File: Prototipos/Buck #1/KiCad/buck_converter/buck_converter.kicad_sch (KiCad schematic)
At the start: 19 parts, among them J1 Screw_Terminal_01x02, J3 Screw_Terminal_01x02, J4 Conn_01x03_Pin, Q1 IRLZ44N, Q2 IRF9540NPBF

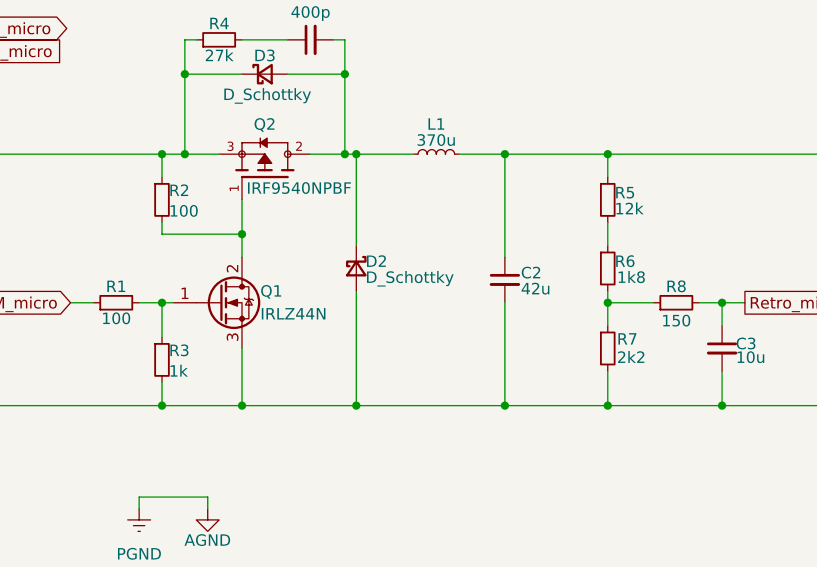
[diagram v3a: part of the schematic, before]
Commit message: Diseño del circuito final, agregado de nuevas librerías
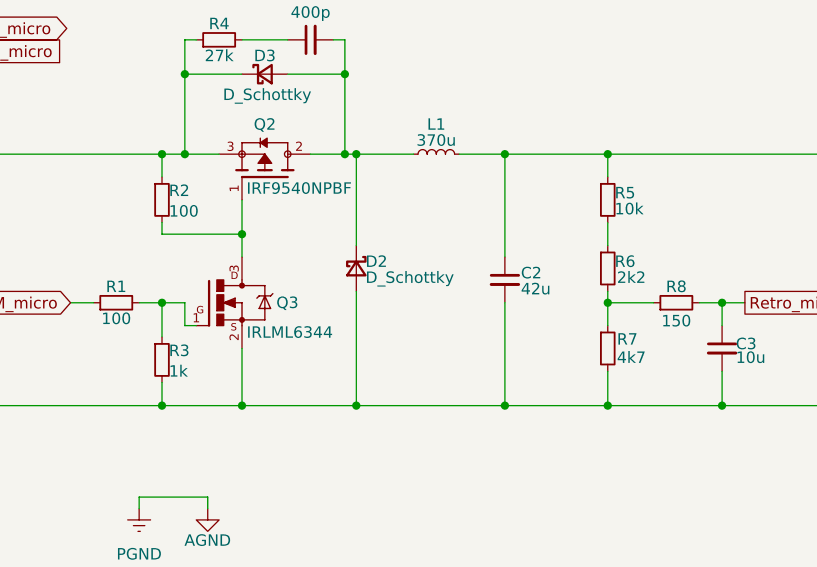
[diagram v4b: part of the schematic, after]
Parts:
- removed Q1: IRLZ44N, Package_TO_SOT_THT:TO-220-3_Vertical, symbol Transistor_FET:IRLZ44N
- added Q3: IRLML6344, IRLML6344:SOT23, symbol IRLML6344:IRLML6344
- R5: value 12k -> 10k
- R6: value 1k8 -> 2k2
- R7: value 2k2 -> 4k7
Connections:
- net AGND: now also Q3.2
- net at Q2.1, R2.2: now also Q3.3
- net at R1.2, R3.1: now also Q3.1
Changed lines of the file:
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@@
 	(wire
 		(pts
-			(xy 86.36 69.85) (xy 87.63 69.85)
+			(xy 86.36 69.85) (xy 88.9 69.85)
 		)
 		(stroke
@@
 	(wire
 		(pts
+			(xy 88.9 72.39) (xy 90.17 72.39)
+		)
+		(stroke
+			(width 0)
+			(type default)
+		)
+	)
+	(wire
+		(pts
 			(xy 135.89 60.96) (xy 135.89 63.5)
 		)
@@
 		(pts
 			(xy 148.59 69.85) (xy 148.59 72.39)
+		)
+		(stroke
+			(width 0)
+			(type default)
+		)
+	)
+	(wire
+		(pts
+			(xy 88.9 69.85) (xy 88.9 72.39)
 		)
 		(stroke
@@
 	)
 	(symbol
+		(lib_id "IRLML6344:IRLML6344")
+		(at 92.71 69.85 0)
+		(unit 1)
+		(exclude_from_sim no)
+		(in_bom yes)
+		(on_board yes)
+		(dnp no)
+		(property "Reference" "Q3"
+			(at 99.06 69.85 0)
+			(effects
+				(font
+					(size 1.27 1.27)
+				)
+				(justify left)
+			)
+		)
+		(property "Value" "IRLML6344"
+			(at 95.758 73.152 0)
+			(effects
+				(font
+					(size 1.27 1.27)
+				)
+				(justify left)
+			)
+		)
+		(property "Footprint" "IRLML6344:SOT23"
+			(at 92.71 69.85 0)
+			(effects
+				(font
+					(size 1.27 1.27)
+				)
+				(justify bottom)
+				(hide yes)
+			)
+		)
+		(property "Datasheet" ""
+			(at 92.71 69.85 0)
+			(effects
+				(font
+					(size 1.27 1.27)
+				)
+				(hide yes)
+			)
+		)
+		(property "Description" ""
+			(at 92.71 69.85 0)
+			(effects
+				(font
+					(size 1.27 1.27)
+				)
+				(hide yes)
+			)
+		)
+		(property "MF" "Infineon Technologies"
+			(at 92.71 69.85 0)
+			(effects
+				(font
+					(size 1.27 1.27)
+				)
+				(justify bottom)
+				(hide yes)
+			)
+		)
+		(property "Description_1" "Trans MOSFET N-CH 30V 5A 3-Pin SOT-23 T/R"
+			(at 92.71 69.85 0)
+			(effects
+				(font
+					(size 1.27 1.27)
+				)
+				(justify bottom)
+				(hide yes)
+			)
+		)
+		(property "Package" "None"
+			(at 92.71 69.85 0)
+			(effects
+				(font
+					(size 1.27 1.27)
+				)
+				(justify bottom)
+				(hide yes)
+			)
+		)
+		(property "Price" "None"
+			(at 92.71 69.85 0)
+			(effects
+				(font
+					(size 1.27 1.27)
+				)
+				(justify bottom)
+				(hide yes)
+			)
+		)
+		(property "SnapEDA_Link" "https://www.snapeda.com/parts/IRLML6344/Infineon/view-part/?ref=snap"
+			(at 92.71 69.85 0)
+			(effects
+				(font
+					(size 1.27 1.27)
+				)
+				(justify bottom)
+				(hide yes)
+			)
+		)
+		(property "MP" "IRLML6344"
+			(at 92.71 69.85 0)
+			(effects
+				(font
+					(size 1.27 1.27)
+				)
+				(justify bottom)
+				(hide yes)
+			)
+		)
+		(property "Availability" "Not in stock"
+			(at 92.71 69.85 0)
+			(effects
+				(font
+					(size 1.27 1.27)
+				)
+				(justify bottom)
+				(hide yes)
+			)
+		)
+		(property "Check_prices" "https://www.snapeda.com/parts/IRLML6344/Infineon/view-part/?ref=eda"
+			(at 92.71 69.85 0)
+			(effects
+				(font
+					(size 1.27 1.27)
+				)
+				(justify bottom)
+				(hide yes)
+			)
+		)
+		(pin "3"
+		)
+		(pin "2"
+		)
+		(pin "1"
+		)
+		(instances
+			(project ""
+				(path "/bb8bc01e-43dc-40c7-9cc7-76fd3e77d2b7"
+					(reference "Q3")
+					(unit 1)
+				)
+			)
+		)
+	)
+	(symbol
 		(lib_id "Device:R_Small")
 		(at 92.71 40.64 90)
@@
 	)
 	(symbol
-		(lib_id "Transistor_FET:IRLZ44N")
-		(at 92.71 69.85 0)
-		(unit 1)
-		(exclude_from_sim no)
-		(in_bom yes)
-		(on_board yes)
-		(dnp no)
-		(property "Reference" "Q1"
-			(at 97.282 68.58 0)
-			(effects
-				(font
-					(size 1.27 1.27)
-				)
-				(justify left)
-			)
-		)
-		(property "Value" "IRLZ44N"
-			(at 97.282 71.12 0)
-			(effects
-				(font
-					(size 1.27 1.27)
-				)
-				(justify left)
-			)
-		)
-		(property "Footprint" "Package_TO_SOT_THT:TO-220-3_Vertical"
-			(at 97.79 71.755 0)
-			(effects
-				(font
-					(size 1.27 1.27)
-					(italic yes)
-				)
-				(justify left)
-				(hide yes)
-			)
-		)
-		(property "Datasheet" "http://www.irf.com/product-info/datasheets/data/irlz44n.pdf"
-			(at 97.79 73.66 0)
-			(effects
-				(font
-					(size 1.27 1.27)
-				)
-				(justify left)
-				(hide yes)
-			)
-		)
-		(property "Description" "47A Id, 55V Vds, 22mOhm Rds Single N-Channel HEXFET Power MOSFET, TO-220AB"
-			(at 92.71 69.85 0)
-			(effects
-				(font
-					(size 1.27 1.27)
-				)
-				(hide yes)
-			)
-		)
-		(pin "1"
-		)
-		(pin "2"
-		)
-		(pin "3"
-		)
-		(instances
-			(project ""
-				(path "/bb8bc01e-43dc-40c7-9cc7-76fd3e77d2b7"
-					(reference "Q1")
-					(unit 1)
-				)
-			)
-		)
-	)
-	(symbol
 		(lib_id "Device:R_Small")
 		(at 135.89 74.93 0)
@@
 			)
 		)
-		(property "Value" "2k2"
+		(property "Value" "4k7"
 			(at 136.906 75.946 0)
 			(effects
@@
 			)
 		)
-		(property "Value" "1k8"
+		(property "Value" "2k2"
 			(at 136.906 67.056 0)
 			(effects
@@
 			)
 		)
-		(property "Value" "12k"
+		(property "Value" "10k"
 			(at 136.652 59.436 0)
 			(effects

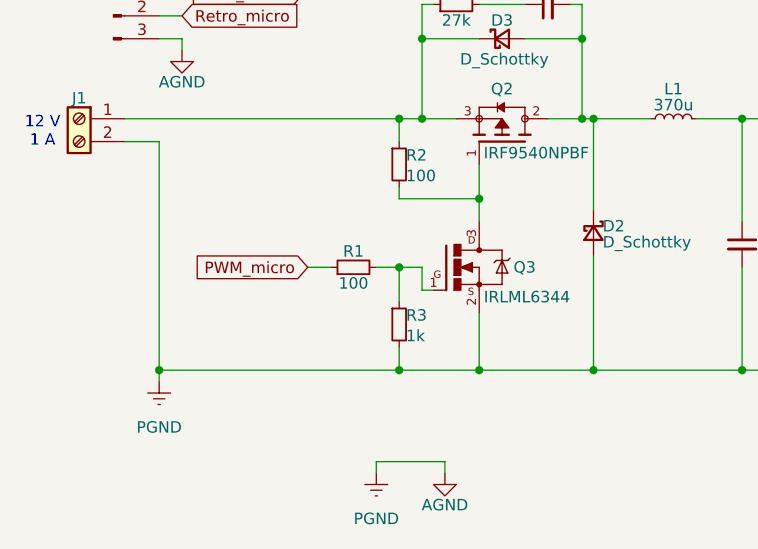
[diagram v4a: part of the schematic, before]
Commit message: Corrección de valor Rg
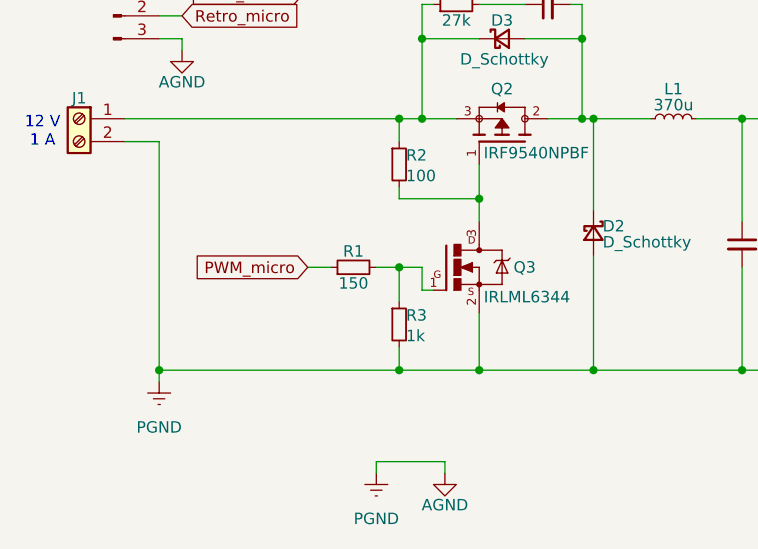
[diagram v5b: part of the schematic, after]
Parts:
- R1: value 100 -> 150
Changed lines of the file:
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@@
 			)
 		)
-		(property "Value" "100"
+		(property "Value" "150"
 			(at 81.28 71.628 90)
 			(effects

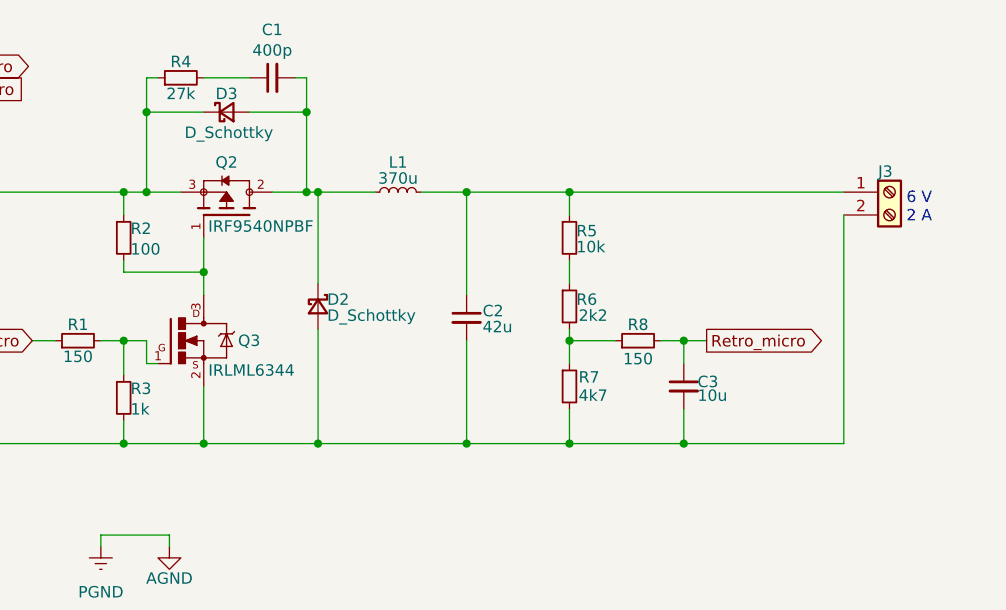
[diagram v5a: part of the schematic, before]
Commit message: Agregado red snubber driver
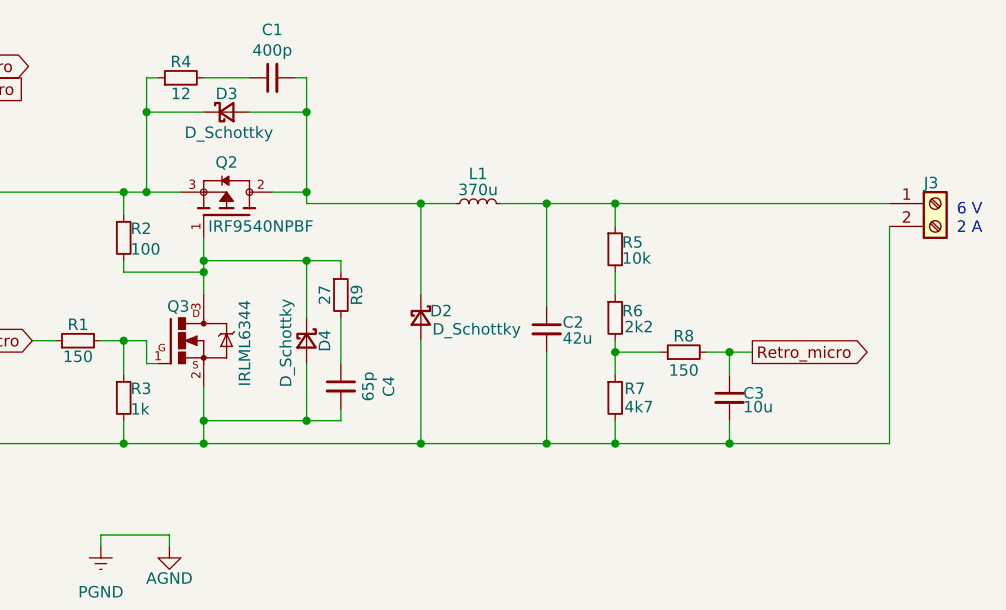
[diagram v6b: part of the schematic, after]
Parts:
- added C4: 65p, Capacitor_THT:C_Disc_D3.8mm_W2.6mm_P2.50mm, symbol Device:C_Small
- added D4: D_Schottky, Diode_THT:D_A-405_P10.16mm_Horizontal, symbol Device:D_Schottky_Small
- added R9: 27, Resistor_THT:R_Axial_DIN0207_L6.3mm_D2.5mm_P15.24mm_Horizontal, symbol Device:R_Small
- R4: value 27k -> 12
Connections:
- net AGND: now also C4.2, D4.2 (A)
- net at Q2.1, Q3.3, R2.2: now also D4.1 (K), R9.1
- new net: C4.1, R9.2
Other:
- moved on the sheet: C2, C3, D2, J3, L1, R5, R6, R7, R8

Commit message: Corrección de valores
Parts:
- added C1: 1u, Capacitor_THT:C_Disc_D3.8mm_W2.6mm_P2.50mm, symbol Device:C_Small
- added C4: ~, Capacitor_THT:C_Disc_D3.8mm_W2.6mm_P2.50mm, symbol Device:C_Small
- added R6: ~, Resistor_THT:R_Axial_DIN0207_L6.3mm_D2.5mm_P15.24mm_Horizontal, symbol Device:R_Small
- renumbered C1 to C2, C4 to C3, C2 to C5, C3 to C6, D3 to D1, D4 to D2, D2 to D3, J4 to J2, Q3 to Q1, R8 to R10, R9 to R5, R5 to R7, R6 to R8, R7 to R9
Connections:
- net AGND: now also C1.2; no longer C3.2, C5.2, C6.2, D2.2 (A), D3.2 (A), J1.2 (Pin_2), J3.2 (Pin_2), Q1.2, R3.2, R9.2
- net at C2.2, D1.2 (A), D3.1 (K)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: now also R6.1
- new net: C4.1, R6.2
- new net PGND: C1.1, C3.2, C4.2, C5.2, C6.2, D2.2 (A), D3.2 (A), J1.2 (Pin_2), J3.2 (Pin_2), Q1.2, R3.2, R9.2
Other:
- note added: "Puede que sea innecesario el capacitor de acople de masas"
- moved on the sheet: D3

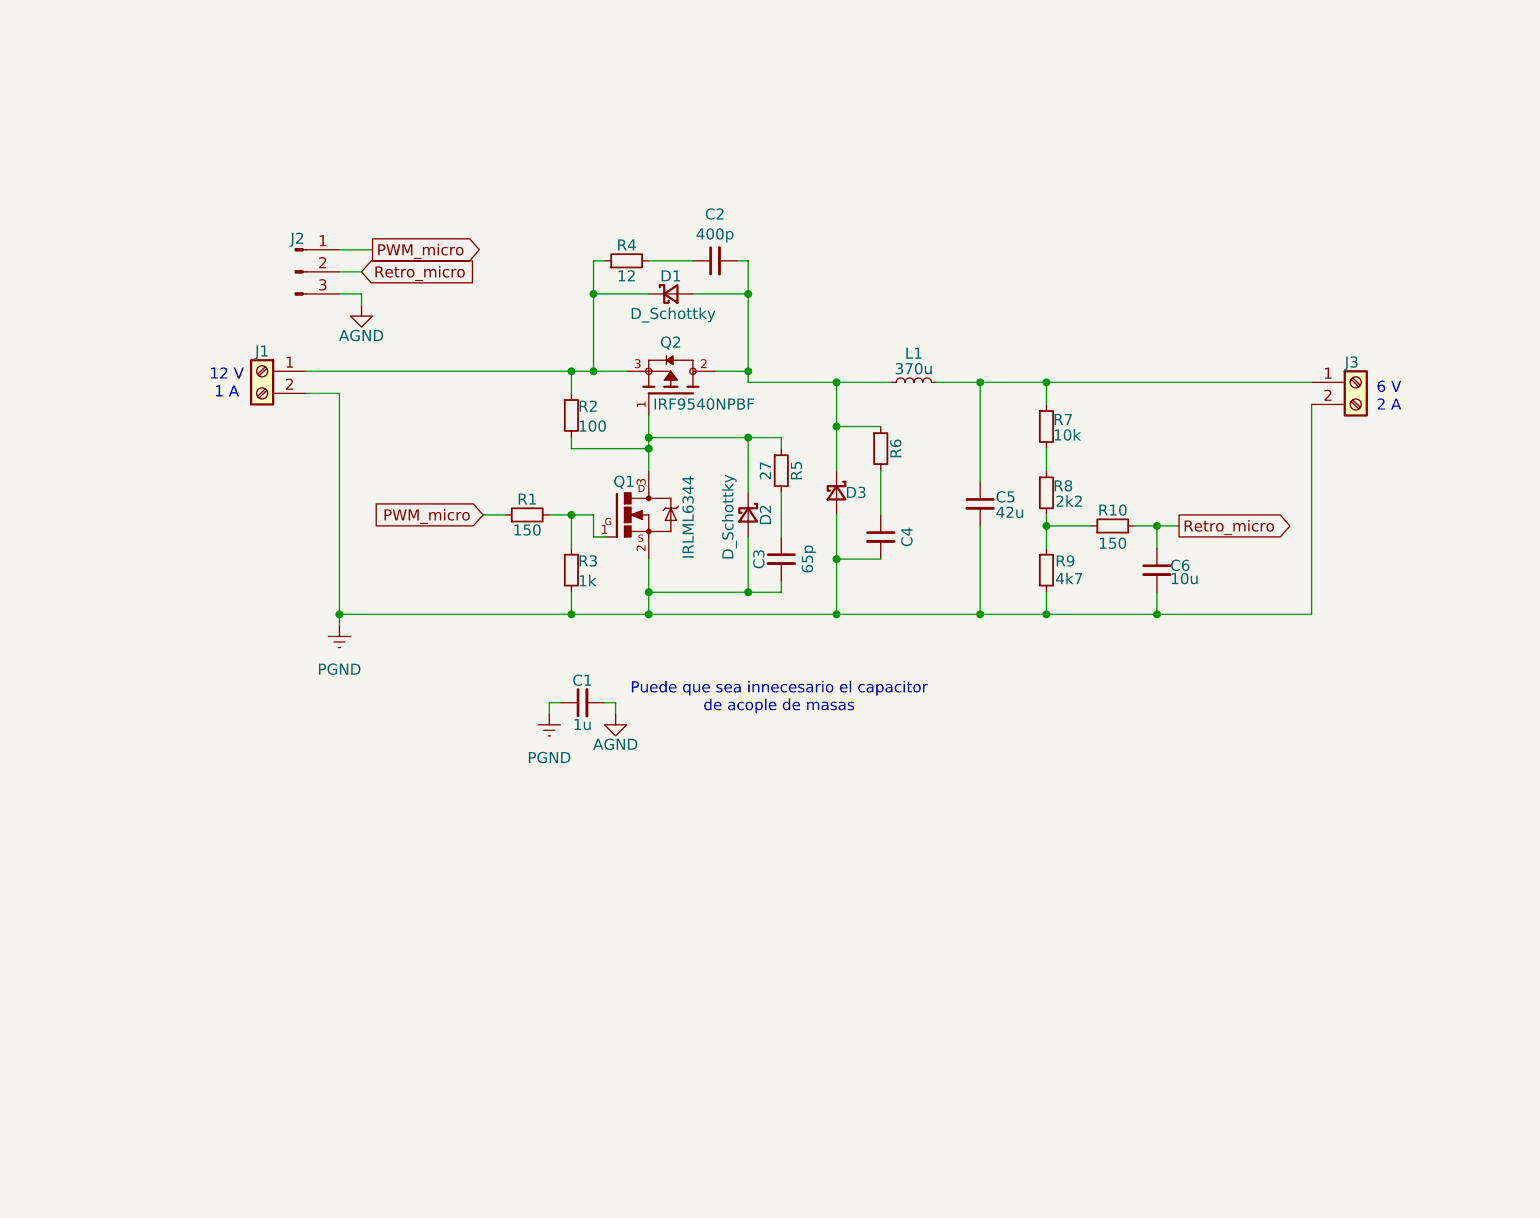
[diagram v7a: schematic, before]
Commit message: Agregado de diseño de disparo con BJT
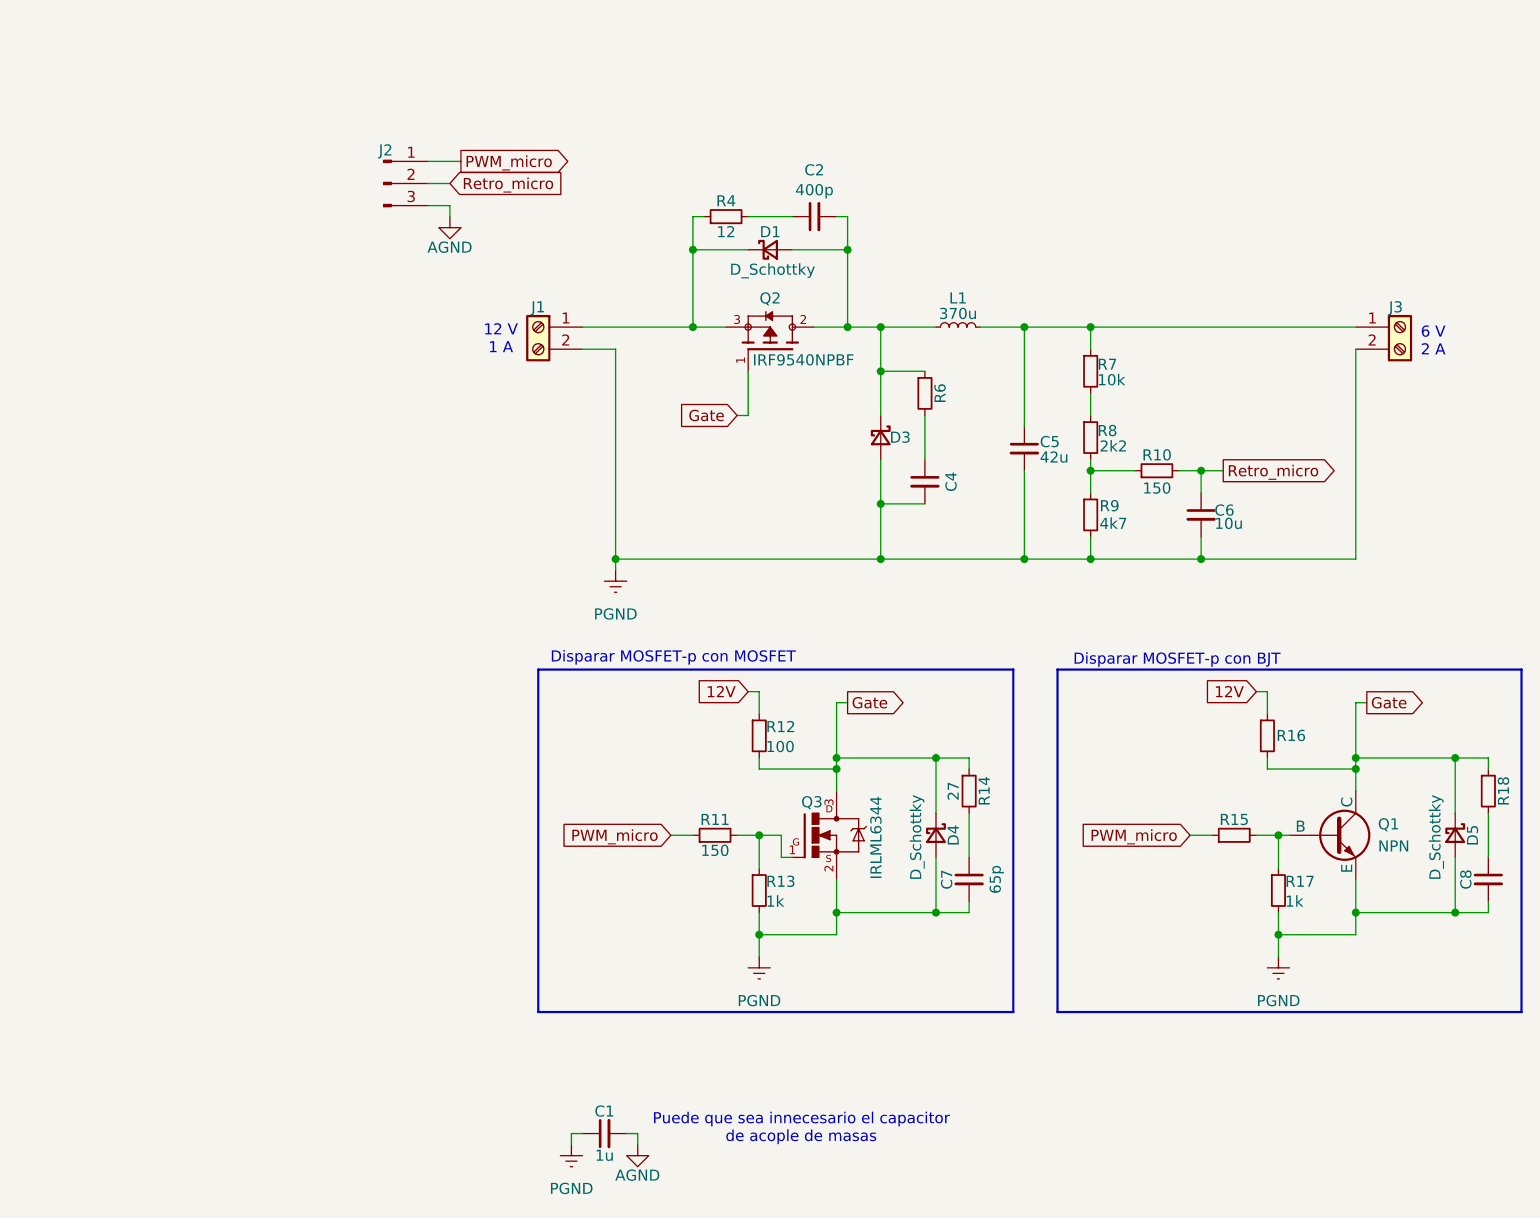
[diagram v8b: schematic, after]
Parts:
- removed C3: 65p, Capacitor_THT:C_Disc_D3.8mm_W2.6mm_P2.50mm, symbol Device:C_Small
- removed D2: D_Schottky, Diode_THT:D_A-405_P10.16mm_Horizontal, symbol Device:D_Schottky_Small
- removed Q1: IRLML6344, IRLML6344:SOT23, symbol IRLML6344:IRLML6344
- removed R1: 150, Resistor_THT:R_Axial_DIN0207_L6.3mm_D2.5mm_P15.24mm_Horizontal, symbol Device:R_Small
- removed R2: 100, Resistor_THT:R_Axial_DIN0207_L6.3mm_D2.5mm_P15.24mm_Horizontal, symbol Device:R_Small
- removed R3: 1k, Resistor_THT:R_Axial_DIN0207_L6.3mm_D2.5mm_P15.24mm_Horizontal, symbol Device:R_Small
- removed R5: 27, Resistor_THT:R_Axial_DIN0207_L6.3mm_D2.5mm_P15.24mm_Horizontal, symbol Device:R_Small
- added C7: 65p, Capacitor_THT:C_Disc_D3.8mm_W2.6mm_P2.50mm, symbol Device:C_Small
- added C8: (no value), Capacitor_THT:C_Disc_D3.8mm_W2.6mm_P2.50mm, symbol Device:C_Small
- added D4, D5: D_Schottky, Diode_THT:D_A-405_P10.16mm_Horizontal, symbol Device:D_Schottky_Small
- added Q1: NPN, symbol Simulation_SPICE:NPN
- added Q3: IRLML6344, IRLML6344:SOT23, symbol IRLML6344:IRLML6344
- added R11: 150, Resistor_THT:R_Axial_DIN0207_L6.3mm_D2.5mm_P15.24mm_Horizontal, symbol Device:R_Small
- added R12: 100, Resistor_THT:R_Axial_DIN0207_L6.3mm_D2.5mm_P15.24mm_Horizontal, symbol Device:R_Small
- added R13, R17: 1k, Resistor_THT:R_Axial_DIN0207_L6.3mm_D2.5mm_P15.24mm_Horizontal, symbol Device:R_Small
- added R14: 27, Resistor_THT:R_Axial_DIN0207_L6.3mm_D2.5mm_P15.24mm_Horizontal, symbol Device:R_Small
- added R15, R16, R18: (no value), Resistor_THT:R_Axial_DIN0207_L6.3mm_D2.5mm_P15.24mm_Horizontal, symbol Device:R_Small
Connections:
- net PGND: now also C7.2, C8.2, D4.2 (A), D5.2 (A), Q1.3 (E), Q3.2, R13.2, R17.2
- net PWM_micro: now also R11.1, R15.1
- net Gate: now reaches Q2.1
- net Gate: now also D4.1 (K), D5.1 (K), Q1.1 (C), Q3.3, R12.2, R14.1, R16.2, R18.1
- new net: Q1.2 (B), R15.2, R17.1
- new net: Q3.1, R11.2, R13.1
- new net: C8.1, R18.2
- new net: C7.1, R14.2
- new net 12V: R12.1, R16.1
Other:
- note added: "Disparar MOSFET-p con BJT"
- note added: "Disparar MOSFET-p con MOSFET"
- moved on the sheet: C1, C2, C4, C5, C6, D1, D3, J1, J2, J3, L1, Q2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
